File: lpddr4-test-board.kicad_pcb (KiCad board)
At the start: 8 copper layers, 117 x 86 mm, 242 parts, among them IC1 TPS54561, IC3 TPD8S009DSMR, J1 0878311420, J10 61300311121, J2 08B0-1X1T-36-F, J3 DC_SOCKET, J4 WE_629105150521, J5 2309409-1, J6 685119134923, J7 1140084168, Q2 BSS138APW, Q3 BSS138APW, Q4 BSS138APW, Q5 BSS138APW, Q6 BSS138APW, Q7 BSS138APW, Q8 BSS138APW, U1 XC7K70T-FBG484, U2 ASEM1-100.000MHZ-LC-T, U3 S25FL128SAGNFI000, U4 TPS65296, U5 TPS62823DLCT, U6 DP83848JSQ_NOPB, U7 FT4232HQ, Y1 ABM8G-25.000MHZ-18-D2Y-T

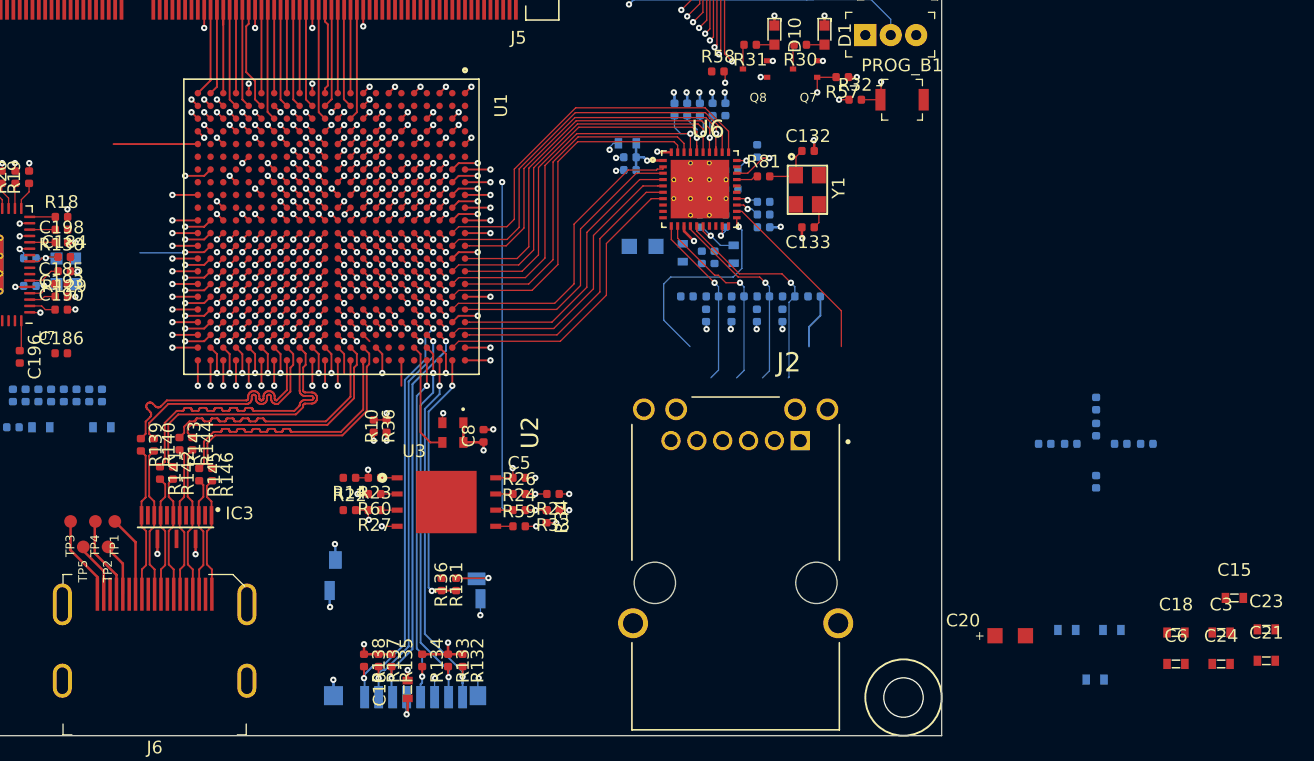
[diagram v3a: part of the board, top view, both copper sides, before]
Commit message: Place and route decoupling capacitors
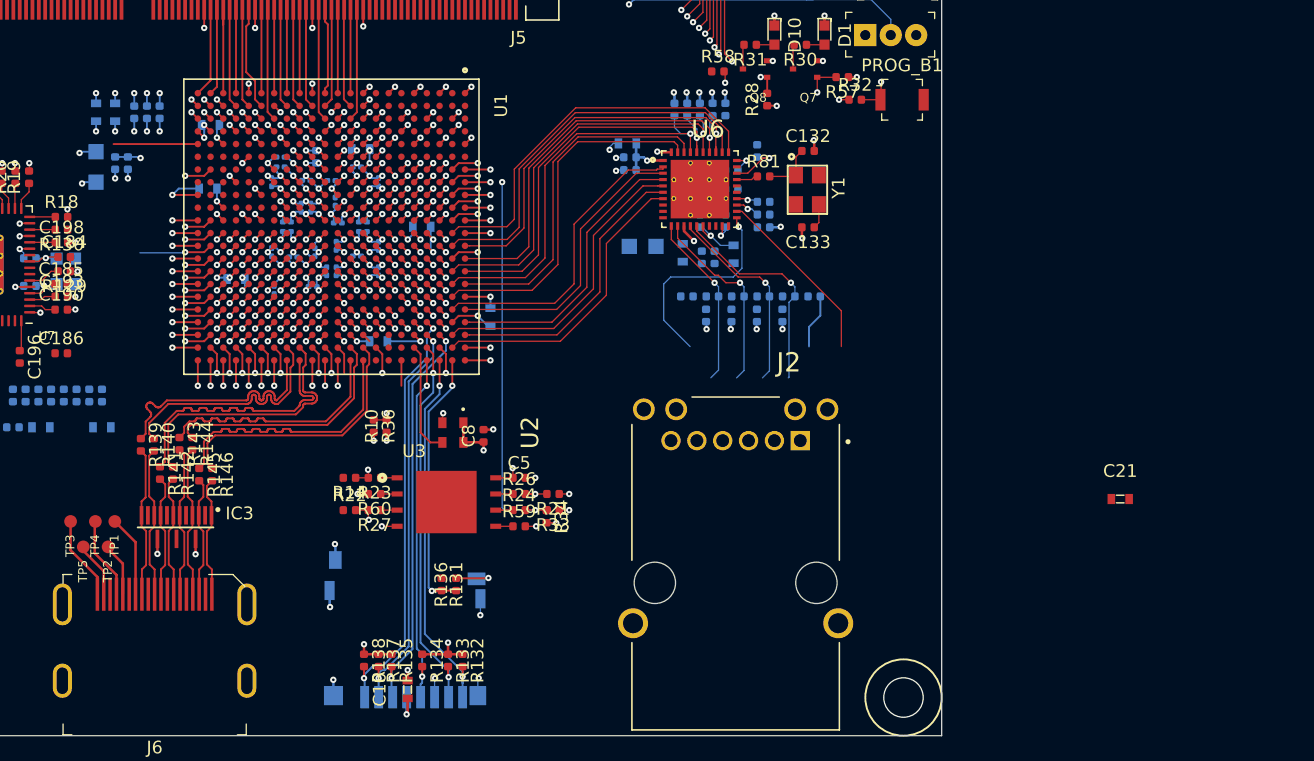
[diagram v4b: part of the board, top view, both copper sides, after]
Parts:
- added C11: C_100n_0201, antmicro-footprints:0201-res, B.Cu at (165.0, 90.5)
- added C47: C_100n_0201, antmicro-footprints:0201-res, B.Cu at (164.3, 92.5)
- added C48: C_100n_0201, antmicro-footprints:0201-res, B.Cu at (171.5, 96.4)
- added C49: C_100n_0201, antmicro-footprints:0201-res, B.Cu at (165.5, 96.4)
- added C50: C_100n_0201, antmicro-footprints:0201-res, B.Cu at (164.3, 98.0)
- added C51: C_100n_0201, antmicro-footprints:0201-res, B.Cu at (166.7, 94.5)
- added C52: C_100n_0201, antmicro-footprints:0201-res, B.Cu at (167.7, 98.0)
- added C53: C_100n_0201, antmicro-footprints:0201-res, B.Cu at (165.0, 91.3)
- added C54: C_100n_0201, antmicro-footprints:0201-res, B.Cu at (169.4, 97.5)
- added C55: C_100n_0201, antmicro-footprints:0201-res, B.Cu at (167.4, 94.5)
- added C56: C_100n_0201, antmicro-footprints:0201-res, B.Cu at (169.5, 95.7)
- added C57: C_100n_0201, antmicro-footprints:0201-res, B.Cu at (172.7, 92.5)
- added C58: C_100n_0201, antmicro-footprints:0201-res, B.Cu at (171.5, 95.6)
- added C59: C_100n_0201, antmicro-footprints:0201-res, B.Cu at (172.7, 97.5)
- added C60: C_100n_0201, antmicro-footprints:0201-res, B.Cu at (172.7, 99.5)
- added C61: C_100n_0201, antmicro-footprints:0201-res, B.Cu at (171.0, 91.3)
- added C62: C_100n_0201, antmicro-footprints:0201-res, B.Cu at (171.0, 98.3)
- added C63: C_100n_0201, antmicro-footprints:0201-res, B.Cu at (169.3, 94.0)
- added C64: C_100n_0201, antmicro-footprints:0201-res, B.Cu at (169.4, 99.5)
- added C65: C_100n_0201, antmicro-footprints:0201-res, B.Cu at (169.0, 92.4)
- added C66: C_100n_0201, antmicro-footprints:0201-res, B.Cu at (168.7, 99.5)
- added C67: C_100n_0201, antmicro-footprints:0201-res, B.Cu at (167.1, 92.3)
- added C68: C_100n_0201, antmicro-footprints:0201-res, B.Cu at (167.6, 100.7)
- added C69: C_100n_0201, antmicro-footprints:0201-res, B.Cu at (166.0, 98.4)
- added C70: C_100n_0201, antmicro-footprints:0201-res, B.Cu at (164.5, 101.0)
- added C9: C_100n_0201, antmicro-footprints:0201-res, B.Cu at (165.5, 95.6)
- C15, C18, C20, C23, C24, C3, C6: moved to B.Cu
- R28: moved to F.Cu
- moved C23 92.0 mm to (159.5, 88.0)
- moved C22 89.6 mm to (150.5, 87.0), turned to 270 degrees
- moved C24 88.0 mm to (159.3, 93.0), turned to 180 degrees
- moved C25 85.2 mm to (152.0, 87.0), turned to 270 degrees
- moved C16 83.7 mm to (153.5, 87.0), turned to 270 degrees
- moved C17 81.1 mm to (153.0, 91.0), turned to 90 degrees
- moved C20 79.1 mm to (150.5, 92.5), turned to 90 degrees
- moved C18 78.9 mm to (161.5, 100.1), turned to 180 degrees
- moved C19 78.0 mm to (154.5, 87.0), turned to 270 degrees
- moved C14 76.3 mm to (152.0, 91.0), turned to 90 degrees
- moved C7 76.2 mm to (155.5, 87.0), turned to 270 degrees
- moved C12 71.2 mm to (171.3, 89.9), turned to 180 degrees
- moved C3 70.5 mm to (176.1, 96.0)
- moved C15 70.2 mm to (172.7, 105.0)
- moved C13 64.9 mm to (167.8, 90.5), turned to 90 degrees
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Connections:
- U1 pad K11: XADCGND -> GND
- U1 pad K12: XADC1V8 -> VCC1V8
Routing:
- net GND: track 173.5 -> 215.3 mm, vias 184 -> 192
- net VCC1V1: track 12.0 -> 27.9 mm, vias 17 -> 20
- net VCC1V8: track 15.0 -> 27.2 mm, vias 8 -> 14
- net VCC3V3: track 74.5 -> 78.5 mm
- net VCC3v3: track 8.15 -> 10.8 mm, vias 11 -> 12
- net VDDQ: track 10.0 -> 12.1 mm
- net INIT_B: track 40.1 -> 41.8 mm
- net XADCGND: track 0.71 -> 0.00 mm, vias 1 -> 0
- net XADC1V8: track 0.71 -> 0.00 mm, vias 1 -> 0

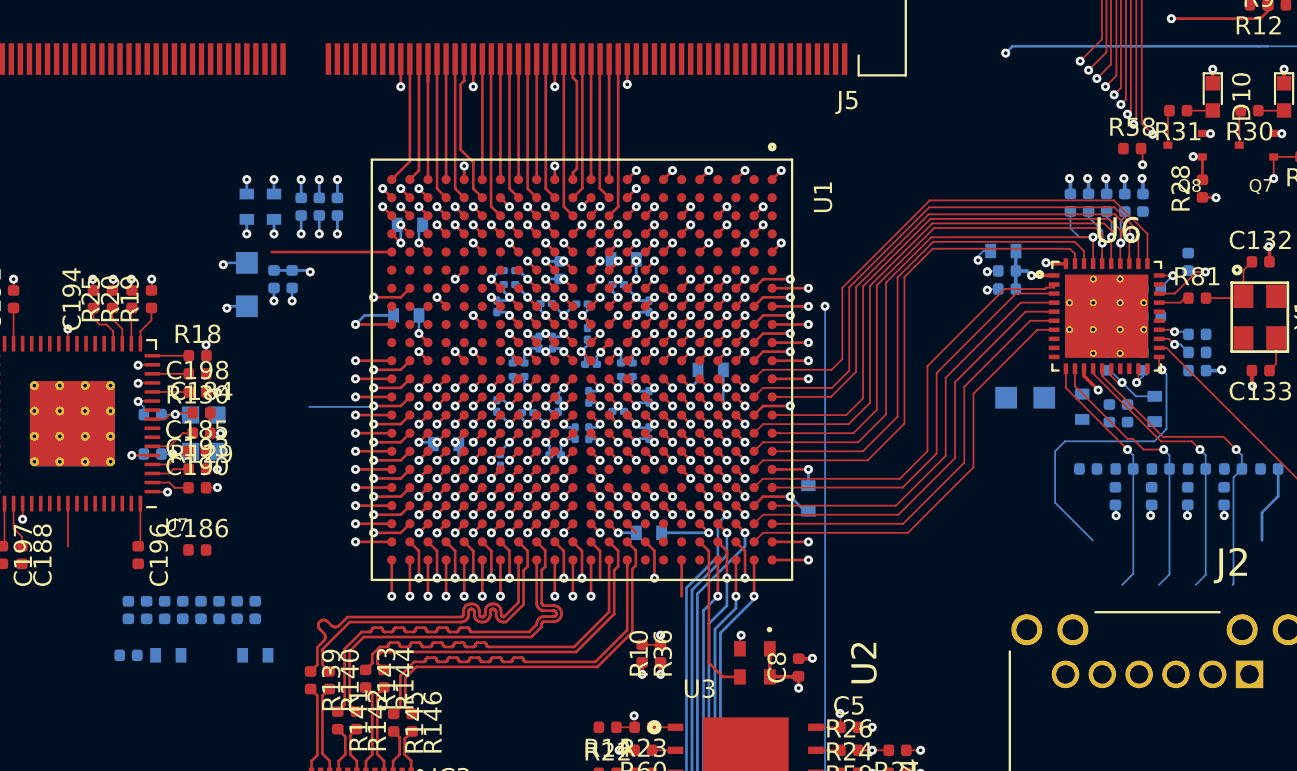
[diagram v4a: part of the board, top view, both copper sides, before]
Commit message: Add FPGA - FTDI JTAG connections
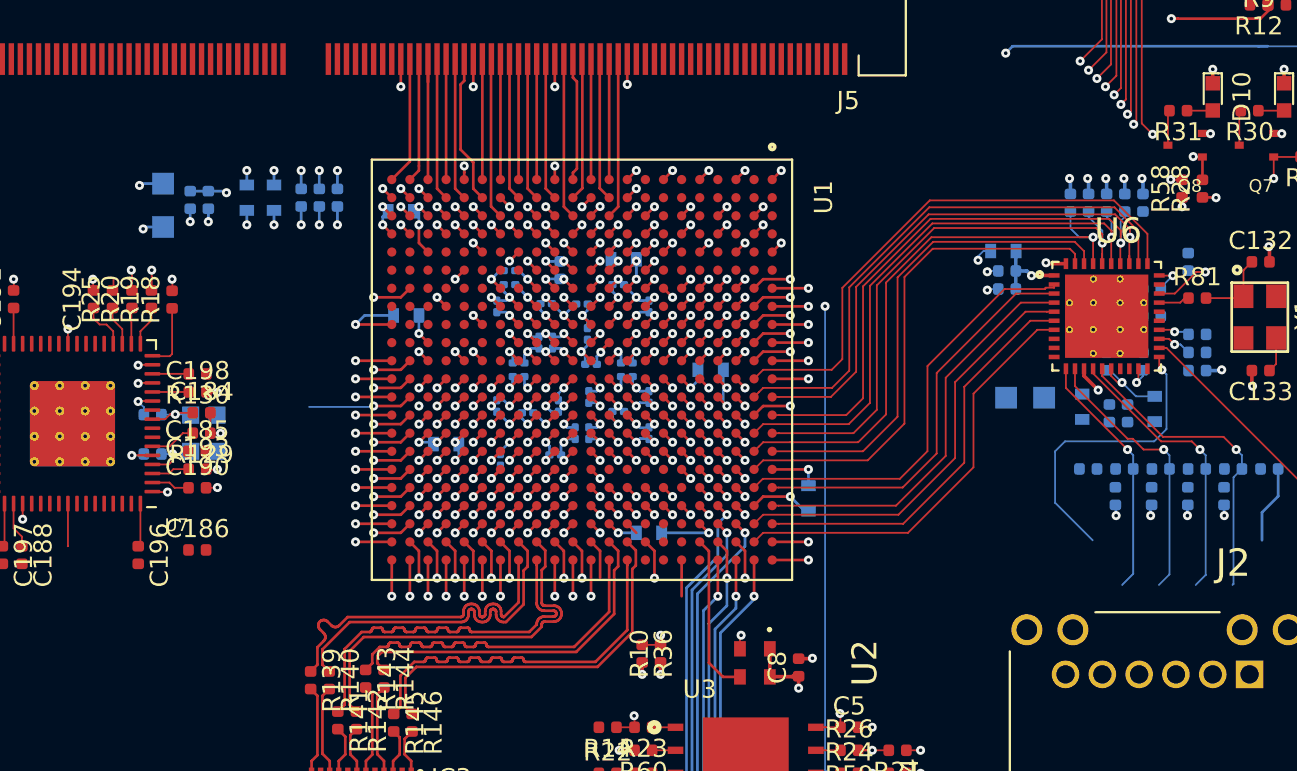
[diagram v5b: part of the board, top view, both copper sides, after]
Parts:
- removed C1: C_910p_0402, lpddr4-test-board-footprints:0402-res
- removed C2, C4: C_1n_0603, lpddr4-test-board-footprints:0603-cap
- removed R1, R2, R3, R4, R5, R6, R7, R8: R_100R_0402, lpddr4-test-board-footprints:0402-res
- moved C14 6.37 mm to (147.4, 86.6)
- moved C17 6.37 mm to (148.4, 86.6)
- moved C20 6.37 mm to (145.9, 88.1)
- moved R58 3.53 mm to (202.2, 86.0), turned to 90 degrees
- moved R18 3.41 mm to (146.4, 92.1), turned to 90 degrees
- moved C23 0.90 mm to (159.0, 87.2)
- moved C16 0.50 mm to (153.5, 86.5)
- moved C19 0.50 mm to (154.5, 86.5)
- moved C22 0.50 mm to (150.5, 86.5)
- moved C25 0.50 mm to (152.0, 86.5)
- moved C7 0.50 mm to (155.5, 86.5)
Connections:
- U1 pad T20: AD9_P -> Net-(U1-PadT20)
- U1 pad U17: AD2_P -> Net-(U1-PadU17)
- U1 pad U18: AD10_N -> Net-(U1-PadU18)
- U1 pad U20: AD1_N -> Net-(U1-PadU20)
- U1 pad V18: AD9_N -> Net-(U1-PadV18)
- U1 pad W21: AD10_P -> Net-(U1-PadW21)
- U1 pad W22: AD2_N -> Net-(U1-PadW22)
- U1 pad Y21: AD1_P -> Net-(U1-PadY21)
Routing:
- net TDO_JTAG: track 52.4 -> 82.3 mm
- net TMS_JTAG: track 53.6 -> 81.7 mm
- net TDI_JTAG: track 54.4 -> 81.9 mm
- net TCK_JTAG: track 52.9 -> 78.9 mm
- net Net-(U1-PadAB5): track 6.62 -> 0.00 mm
- net CFGBVS: track 39.7 -> 41.9 mm
- net Net-(U1-PadY21): track 0.00 -> 2.21 mm, vias 0 -> 1
- net Net-(U1-PadW21): track 0.00 -> 2.21 mm, vias 0 -> 1
- net AD1_P: track 2.21 -> 0.00 mm, vias 1 -> 0
- net AD10_P: track 2.21 -> 0.00 mm, vias 1 -> 0
- net Net-(U1-PadW22): track 0.00 -> 2.00 mm, vias 0 -> 1
- net AD2_N: track 2.00 -> 0.00 mm, vias 1 -> 0
- net Net-(R18-Pad1): track 2.01 -> 3.66 mm
- net Net-(U1-PadV18): track 0.00 -> 0.71 mm, vias 0 -> 1
- net AD9_N: track 0.71 -> 0.00 mm, vias 1 -> 0
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
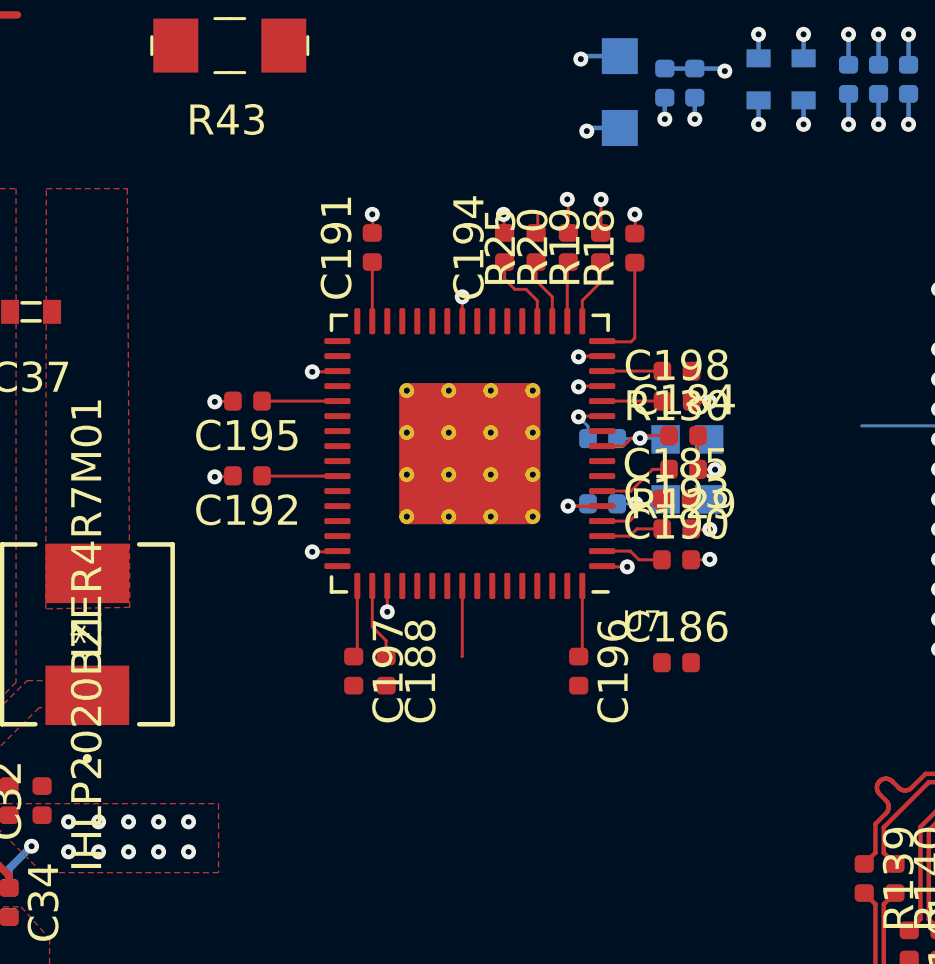
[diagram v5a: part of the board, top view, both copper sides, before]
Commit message: Rotate U7 for better signal alignment
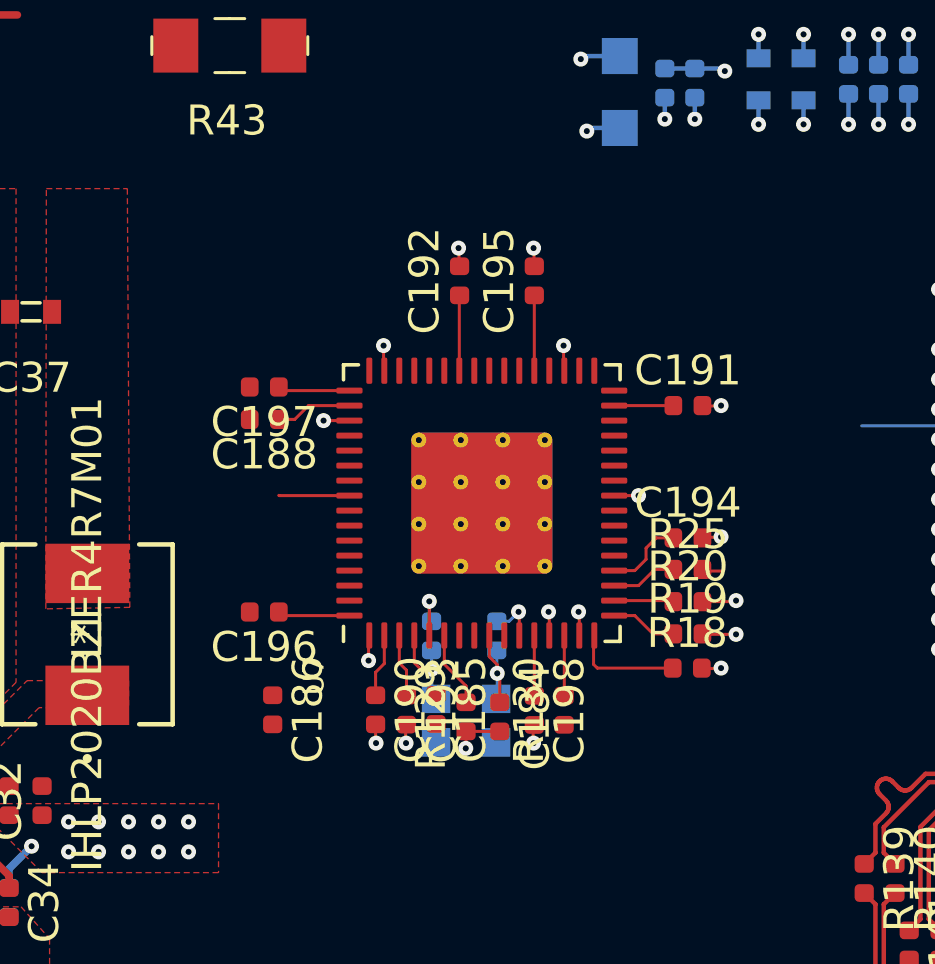
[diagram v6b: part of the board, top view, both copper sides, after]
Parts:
- moved R18 14.1 mm to (148.2, 106.1), turned to 0 degrees
- moved C186 13.6 mm to (134.3, 107.5), turned to 270 degrees
- moved R19 13.2 mm to (148.2, 105.0), turned to 0 degrees
- moved R20 12.5 mm to (148.2, 103.9), turned to 0 degrees
- moved R130 11.9 mm to (144.1, 107.5), turned to 90 degrees
- moved R25 11.9 mm to (148.2, 102.8), turned to 0 degrees
- moved C191 11.8 mm to (148.2, 97.4), turned to 0 degrees
- moved C194 11.4 mm to (148.2, 101.8), turned to 0 degrees
- moved C198 11.4 mm to (143.1, 107.5), turned to 270 degrees
- moved FB4 11.3 mm to (141.8, 107.9), turned to 90 degrees
- moved C190 11.2 mm to (137.8, 107.5), turned to 270 degrees
- moved C184 11.2 mm to (141.9, 107.7), turned to 270 degrees
- moved FB5 11.2 mm to (139.8, 107.9), turned to 90 degrees
- moved R129 11.0 mm to (140.8, 107.7), turned to 90 degrees
- moved C193 10.8 mm to (138.8, 107.5), turned to 270 degrees
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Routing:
- net TCK_JTAG: track 78.9 -> 76.5 mm
- net TDO_JTAG: track 82.3 -> 80.2 mm
- net TDI_JTAG: track 81.9 -> 79.8 mm
- net TMS_JTAG: track 81.7 -> 79.6 mm
